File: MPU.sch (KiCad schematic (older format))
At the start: 19 parts, among them J2 Conn_02x10_Counter_Clockwise, J3 Micro_SD_Card, J4 USB_A, J5 USB_A, SW1 SW_DIP_x03, U1 STM32MP151AAB3, Y1 Crystal_GND24, Y2 Crystal_GND24

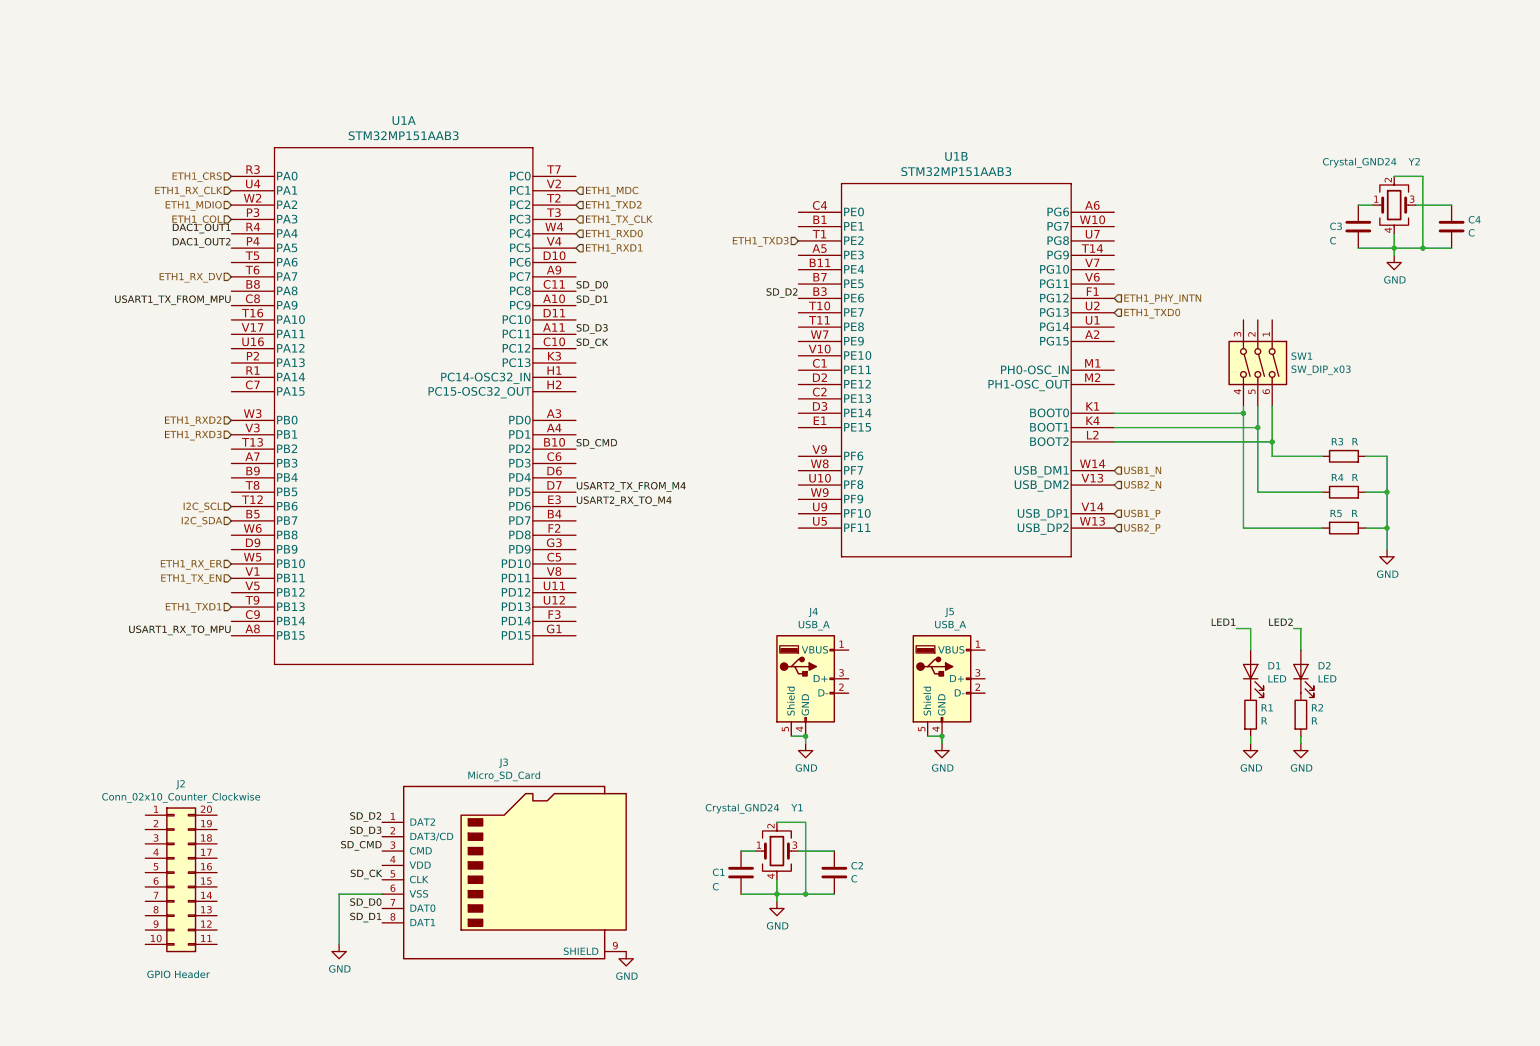
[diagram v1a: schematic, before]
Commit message: Complete ethernet and PMIC circuitry
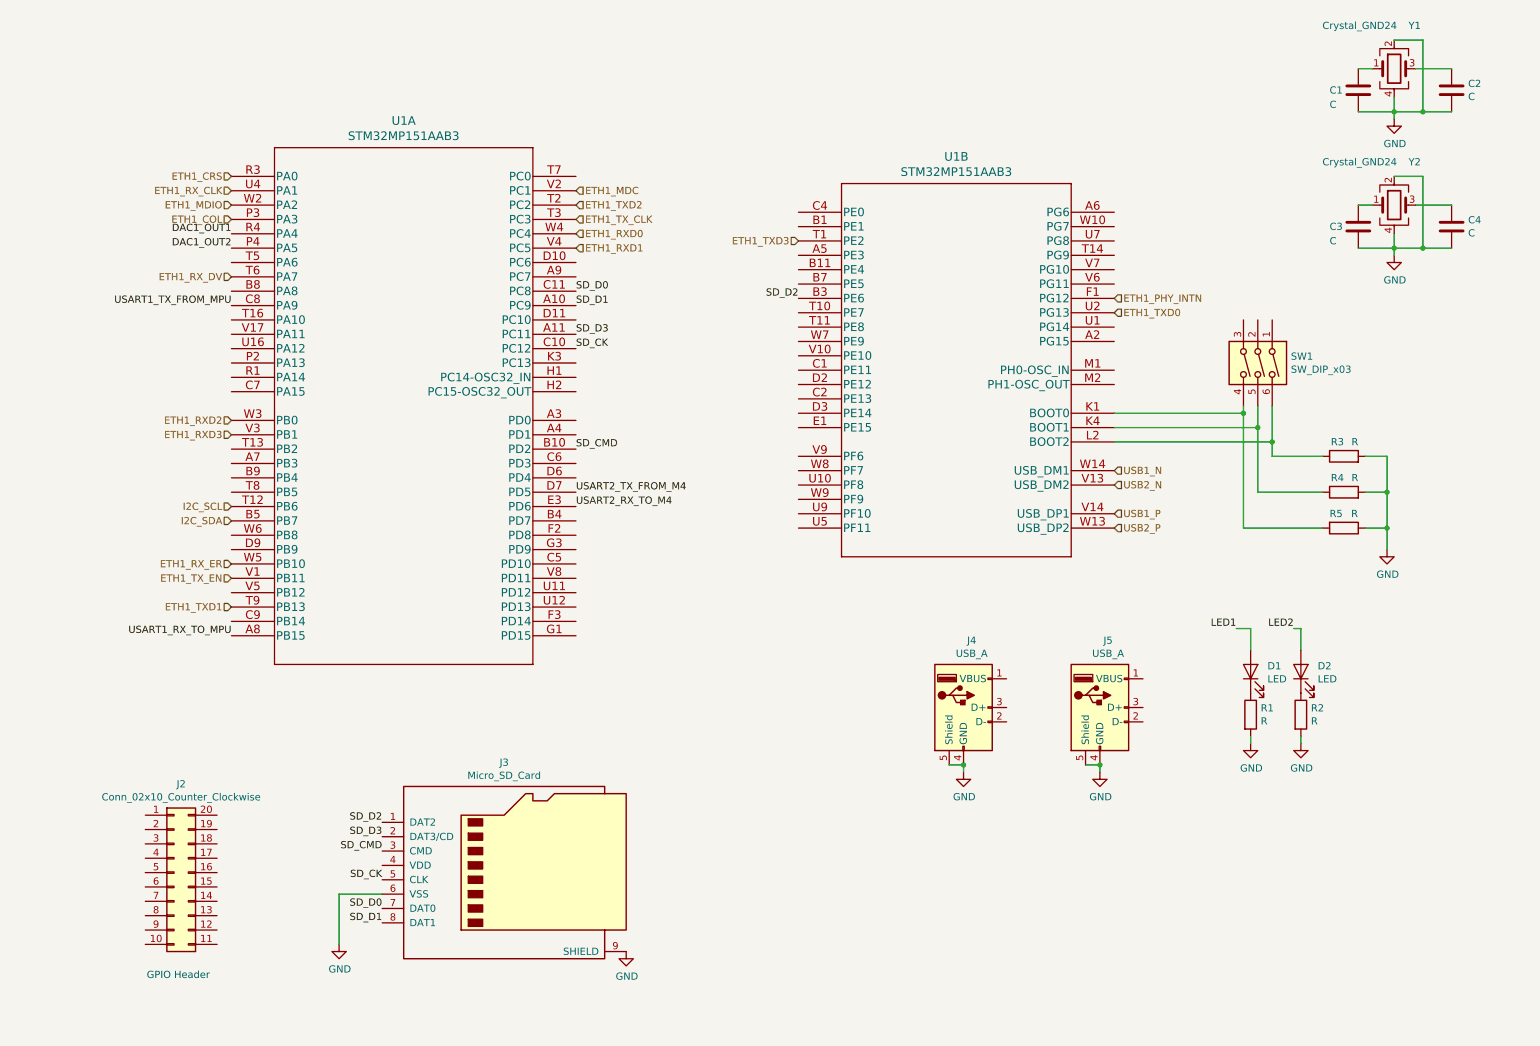
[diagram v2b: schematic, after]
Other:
- moved on the sheet: C1, C2, J4, J5, Y1
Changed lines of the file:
@@
 L Device:Crystal_GND24 Y1
 U 1 1 6061525C
-P 5850 6400
-F 0 "Y1" H 5950 6700 50  0000 L CNN
-F 1 "Crystal_GND24" H 5350 6700 50  0000 L CNN
-F 2 "Crystal:Crystal_SMD_2520-4Pin_2.5x2.0mm" H 5850 6400 50  0001 C CNN
-F 3 "~" H 5850 6400 50  0001 C CNN
-	1    5850 6400
+P 10150 950
+F 0 "Y1" H 10250 1250 50  0000 L CNN
+F 1 "Crystal_GND24" H 9650 1250 50  0000 L CNN
+F 2 "Crystal:Crystal_SMD_2520-4Pin_2.5x2.0mm" H 10150 950 50  0001 C CNN
+F 3 "~" H 10150 950 50  0001 C CNN
+	1    10150 950
 	1    0    0    -1
 $EndComp
@@
 GPIO Header\n
 Wire Wire Line
-	5850 6200 6050 6200
-Wire Wire Line
-	6050 6200 6050 6700
-Wire Wire Line
-	6050 6700 5850 6700
-Wire Wire Line
-	5850 6700 5850 6600
+	10150 750  10350 750
+Wire Wire Line
+	10350 750  10350 1250
+Wire Wire Line
+	10350 1250 10150 1250
+Wire Wire Line
+	10150 1250 10150 1150
 $Comp
 L power:GND #PWR03
 U 1 1 61194FE7
-P 5850 6750
-F 0 "#PWR03" H 5850 6500 50  0001 C CNN
-F 1 "GND" H 5855 6577 50  0000 C CNN
-F 2 "" H 5850 6750 50  0001 C CNN
-F 3 "" H 5850 6750 50  0001 C CNN
-	1    5850 6750
-	1    0    0    -1
-$EndComp
-Wire Wire Line
-	5850 6750 5850 6700
-Connection ~ 5850 6700
+P 10150 1300
+F 0 "#PWR03" H 10150 1050 50  0001 C CNN
+F 1 "GND" H 10155 1127 50  0000 C CNN
+F 2 "" H 10150 1300 50  0001 C CNN
+F 3 "" H 10150 1300 50  0001 C CNN
+	1    10150 1300
+	1    0    0    -1
+$EndComp
+Wire Wire Line
+	10150 1300 10150 1250
+Connection ~ 10150 1250
 $Comp
 L Device:C C2
 U 1 1 61197B94
-P 6250 6550
-F 0 "C2" H 6365 6596 50  0000 L CNN
-F 1 "C" H 6365 6505 50  0000 L CNN
-F 2 "Capacitor_SMD:C_0603_1608Metric" H 6288 6400 50  0001 C CNN
-F 3 "~" H 6250 6550 50  0001 C CNN
-	1    6250 6550
-	1    0    0    -1
-$EndComp
-Wire Wire Line
-	6050 6700 6250 6700
-Connection ~ 6050 6700
-Wire Wire Line
-	6000 6400 6250 6400
-Wire Wire Line
-	5600 6400 5700 6400
-Wire Wire Line
-	5600 6700 5850 6700
+P 10550 1100
+F 0 "C2" H 10665 1146 50  0000 L CNN
+F 1 "C" H 10665 1055 50  0000 L CNN
+F 2 "Capacitor_SMD:C_0603_1608Metric" H 10588 950 50  0001 C CNN
+F 3 "~" H 10550 1100 50  0001 C CNN
+	1    10550 1100
+	1    0    0    -1
+$EndComp
+Wire Wire Line
+	10350 1250 10550 1250
+Connection ~ 10350 1250
+Wire Wire Line
+	10300 950  10550 950
+Wire Wire Line
+	9900 950  10000 950
+Wire Wire Line
+	9900 1250 10150 1250
 $Comp
 L Device:C C1
 U 1 1 6119821B
-P 5600 6550
-F 0 "C1" H 5400 6550 50  0000 L CNN
-F 1 "C" H 5400 6450 50  0000 L CNN
-F 2 "Capacitor_SMD:C_0603_1608Metric" H 5638 6400 50  0001 C CNN
-F 3 "~" H 5600 6550 50  0001 C CNN
-	1    5600 6550
+P 9900 1100
+F 0 "C1" H 9700 1100 50  0000 L CNN
+F 1 "C" H 9700 1000 50  0000 L CNN
+F 2 "Capacitor_SMD:C_0603_1608Metric" H 9938 950 50  0001 C CNN
+F 3 "~" H 9900 1100 50  0001 C CNN
+	1    9900 1100
 	1    0    0    -1
 $EndComp
@@
 L Connector:USB_A J4
 U 1 1 612273A9
-P 6050 5200
-F 0 "J4" H 6107 5667 50  0000 C CNN
-F 1 "USB_A" H 6107 5576 50  0000 C CNN
-F 2 "Connector_USB:USB_A_CNCTech_1001-011-01101_Horizontal" H 6200 5150 50  0001 C CNN
-F 3 " ~" H 6200 5150 50  0001 C CNN
-	1    6050 5200
+P 7150 5400
+F 0 "J4" H 7207 5867 50  0000 C CNN
+F 1 "USB_A" H 7207 5776 50  0000 C CNN
+F 2 "Connector_USB:USB_A_CNCTech_1001-011-01101_Horizontal" H 7300 5350 50  0001 C CNN
+F 3 " ~" H 7300 5350 50  0001 C CNN
+	1    7150 5400
 	1    0    0    -1
 $EndComp
@@
 L Connector:USB_A J5
 U 1 1 612403B4
-P 7000 5200
-F 0 "J5" H 7057 5667 50  0000 C CNN
-F 1 "USB_A" H 7057 5576 50  0000 C CNN
-F 2 "Connector_USB:USB_A_CNCTech_1001-011-01101_Horizontal" H 7150 5150 50  0001 C CNN
-F 3 " ~" H 7150 5150 50  0001 C CNN
-	1    7000 5200
-	1    0    0    -1
-$EndComp
-Wire Wire Line
-	5950 5600 6050 5600
-Wire Wire Line
-	6900 5600 7000 5600
+P 8100 5400
+F 0 "J5" H 8157 5867 50  0000 C CNN
+F 1 "USB_A" H 8157 5776 50  0000 C CNN
+F 2 "Connector_USB:USB_A_CNCTech_1001-011-01101_Horizontal" H 8250 5350 50  0001 C CNN
+F 3 " ~" H 8250 5350 50  0001 C CNN
+	1    8100 5400
+	1    0    0    -1
+$EndComp
+Wire Wire Line
+	7050 5800 7150 5800
+Wire Wire Line
+	8000 5800 8100 5800
 $Comp
 L power:GND #PWR04
 U 1 1 6125217E
-P 6050 5650
-F 0 "#PWR04" H 6050 5400 50  0001 C CNN
-F 1 "GND" H 6055 5477 50  0000 C CNN
-F 2 "" H 6050 5650 50  0001 C CNN
-F 3 "" H 6050 5650 50  0001 C CNN
-	1    6050 5650
-	1    0    0    -1
-$EndComp
-Wire Wire Line
-	6050 5650 6050 5600
-Connection ~ 6050 5600
+P 7150 5850
+F 0 "#PWR04" H 7150 5600 50  0001 C CNN
+F 1 "GND" H 7155 5677 50  0000 C CNN
+F 2 "" H 7150 5850 50  0001 C CNN
+F 3 "" H 7150 5850 50  0001 C CNN
+	1    7150 5850
+	1    0    0    -1
+$EndComp
+Wire Wire Line
+	7150 5850 7150 5800
+Connection ~ 7150 5800
 $Comp
 L power:GND #PWR05
 U 1 1 61254080
-P 7000 5650
-F 0 "#PWR05" H 7000 5400 50  0001 C CNN
-F 1 "GND" H 7005 5477 50  0000 C CNN
-F 2 "" H 7000 5650 50  0001 C CNN
-F 3 "" H 7000 5650 50  0001 C CNN
-	1    7000 5650
-	1    0    0    -1
-$EndComp
-Wire Wire Line
-	7000 5650 7000 5600
-Connection ~ 7000 5600
+P 8100 5850
+F 0 "#PWR05" H 8100 5600 50  0001 C CNN
+F 1 "GND" H 8105 5677 50  0000 C CNN
+F 2 "" H 8100 5850 50  0001 C CNN
+F 3 "" H 8100 5850 50  0001 C CNN
+	1    8100 5850
+	1    0    0    -1
+$EndComp
+Wire Wire Line
+	8100 5850 8100 5800
+Connection ~ 8100 5800
 $EndSCHEMATC

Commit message: Finish labelling RAM
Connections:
- net BOOT0: now reaches R5.2, SW1.4, U1.K1 (BOOT0)
- net BOOT1: now reaches R4.1, SW1.5, U1.K4 (BOOT1)
- net BOOT2: now reaches R3.1, SW1.6, U1.L2 (BOOT2)
- net VDD: now reaches SW1.1
- net VDD: now also SW1.2, SW1.3
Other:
- moved on the sheet: D1, D2, J2, J3, J4, J5, R1, R2, R3, R4, R5, SW1

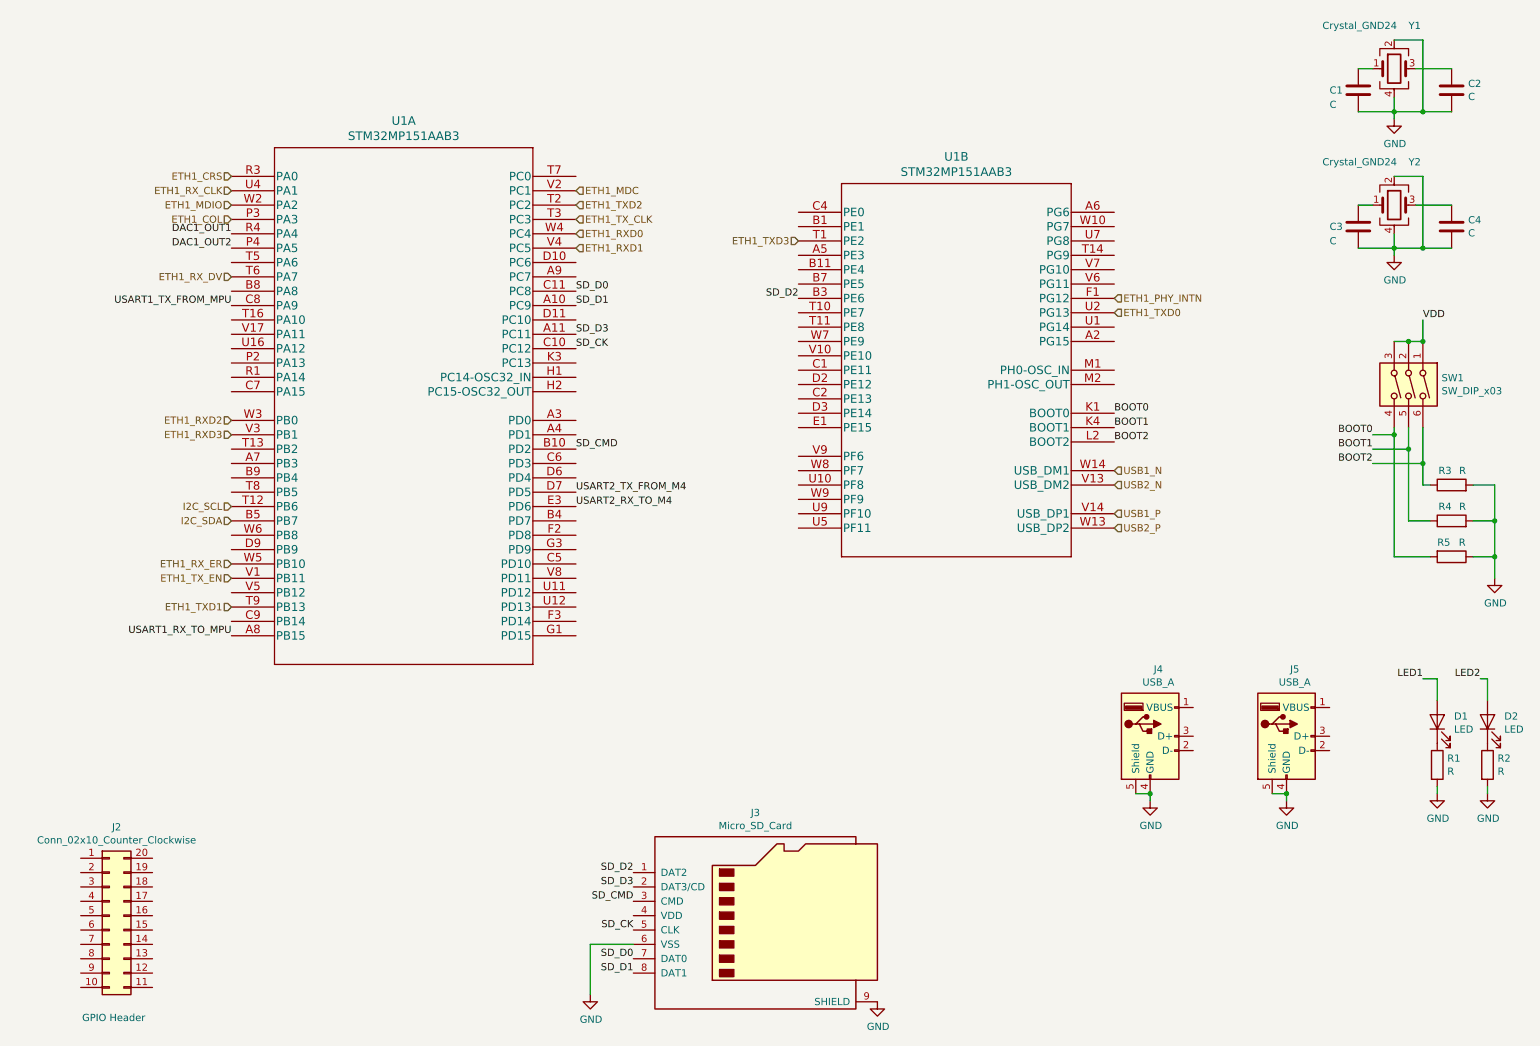
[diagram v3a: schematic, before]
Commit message: Finish DDR schematic
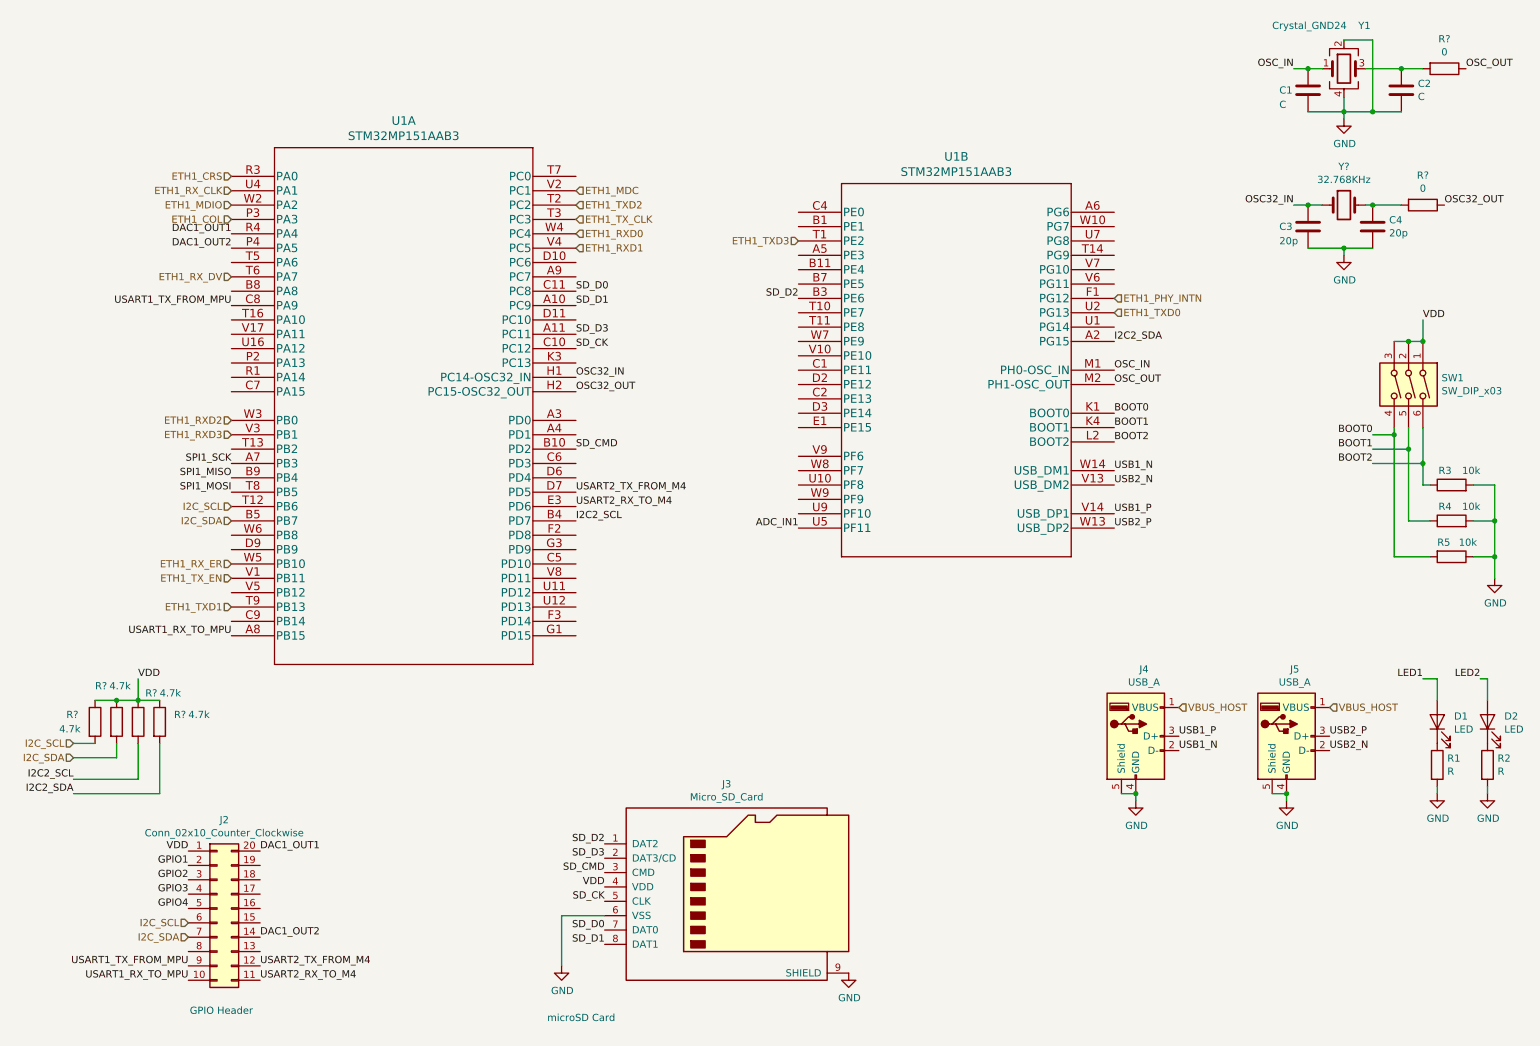
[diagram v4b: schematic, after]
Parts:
- removed Y2: Crystal_GND24, Crystal:Crystal_SMD_2520-4Pin_2.5x2.0mm, symbol Device:Crystal_GND24
- added R? (x2): 0, symbol Device:R
- added R? (x4): 4.7k, symbol Device:R
- added Y?: 32.768KHz, symbol Device:Crystal
- C3, C4: value C -> 20p
- R3, R4, R5: value R -> 10k
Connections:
- net DAC1_OUT1: now also J2.20 (Pin_20)
- net DAC1_OUT2: now also J2.14 (Pin_14)
- net I2C_SCL: now also J2.6 (Pin_6), R?.2
- net I2C_SDA: now also J2.7 (Pin_7), R?.2
- net USART1_RX_TO_MPU: now also J2.10 (Pin_10)
- net USART1_TX_FROM_MPU: now also J2.9 (Pin_9)
- net USART2_RX_TO_M4: now also J2.11 (Pin_11)
- net USART2_TX_FROM_M4: now also J2.12 (Pin_12)
- net USB1_N: now also J4.2 (D-)
- net USB1_P: now also J4.3 (D+)
- net USB2_N: now also J5.2 (D-)
- net USB2_P: now also J5.3 (D+)
- net VDD: now also J2.1 (Pin_1), J3.4 (VDD), R?.1, R?.1, R?.1, R?.1
- net SPI1_SCK: now reaches U1.A7 (PB3)
- net I2C2_SCL: now reaches U1.B4 (PD7)
- net I2C2_SCL: now also R?.2
- net SPI1_MISO: now reaches U1.B9 (PB4)
- net OSC32_IN: now reaches U1.H1 (PC14-OSC32_IN)
- net OSC32_IN: now also C3.1, Y?.1
- net OSC32_OUT: now reaches U1.H2 (PC15-OSC32_OUT)
- net OSC32_OUT: now also R?.1
- net SPI1_MOSI: now reaches U1.T8 (PB5)
- net I2C2_SDA: now reaches U1.A2 (PG15)
- net I2C2_SDA: now also R?.2
- net OSC_IN: now reaches U1.M1 (PH0-OSC_IN)
- net OSC_IN: now also C1.1, Y1.1
- net OSC_OUT: now reaches U1.M2 (PH1-OSC_OUT)
- net OSC_OUT: now also R?.1
- net ADC_IN1: now reaches U1.U5 (PF11)
- net at C2.1, Y1.3: now also R?.2
- net GPIO1: now reaches J2.2 (Pin_2)
- net GPIO2: now reaches J2.3 (Pin_3)
- net GPIO3: now reaches J2.4 (Pin_4)
- net GPIO4: now reaches J2.5 (Pin_5)
- net at C4.1: now also R?.2, Y?.2
- net VBUS_HOST: now reaches J4.1 (VBUS)
- net VBUS_HOST: now also J5.1 (VBUS)
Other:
- note added: "microSD Card\n"
- moved on the sheet: C1, C2, C3, C4, J2, J3, J4, Y1
